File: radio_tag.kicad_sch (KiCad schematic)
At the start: 15 parts, among them U1 MICRF113, Y1 9M84375

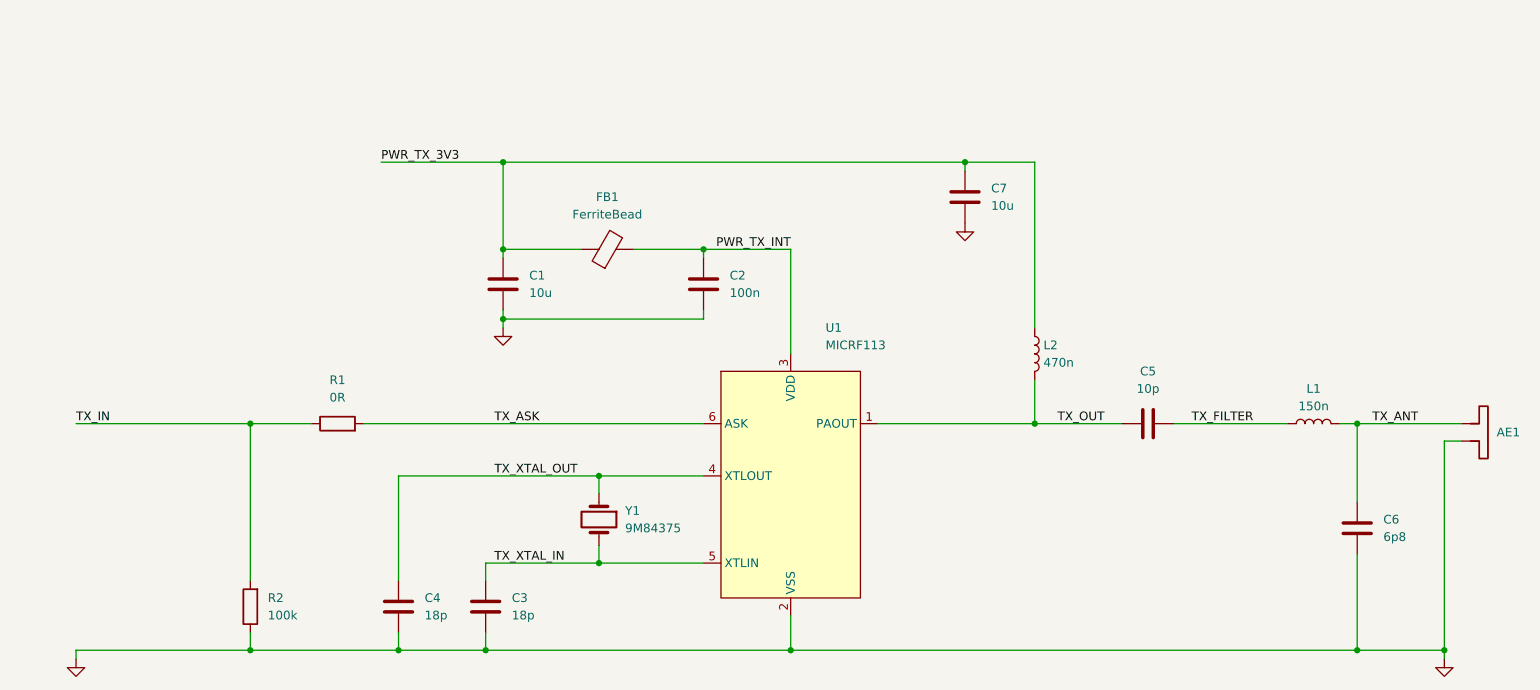
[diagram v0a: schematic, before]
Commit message: Add regulator and complete PN selection
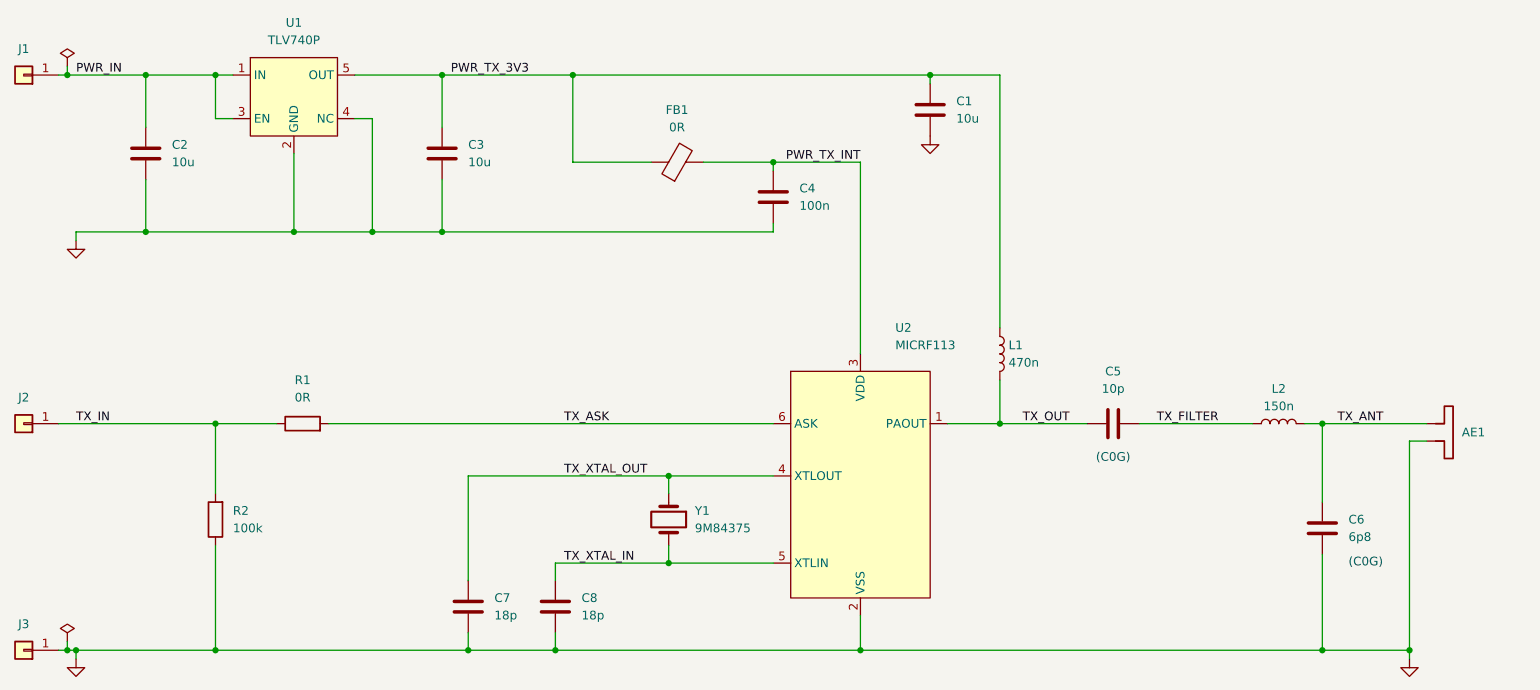
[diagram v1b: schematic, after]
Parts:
- removed C1: 10u, symbol Device:C
- added C2, C3: 10u, Capacitor_SMD:C_0805_2012Metric, symbol Device:C
- added J1, J2, J3: Conn_01x01, Connector_PinHeader_2.54mm:PinHeader_1x01_P2.54mm_Vertical, symbol Connector_Generic:Conn_01x01
- added U1: TLV740P, Package_TO_SOT_SMD:SOT-23-5, symbol regulators:TLV740P
- AE1: footprint (none) -> RF_Antenna:Texas_SWRA117D_2.4GHz_Left; now left out of the parts list
- C1: renamed from C7; footprint (none) -> Capacitor_SMD:C_0805_2012Metric; Manufacturer (none) -> Samsung Electro-mechanics; Manufacturer PN (none) -> CL21A106KOQNNNG; Supplier  (none) -> Digi-Key; Supplier PN (none) -> 1276-6455-1-ND
- C4: renamed from C2; footprint (none) -> Capacitor_SMD:C_0805_2012Metric; Manufacturer (none) -> YAGEO; Manufacturer PN (none) -> CC0805KRX7R9BB104; Supplier  (none) -> Digi-Key; Supplier PN (none) -> 311-1140-1-ND
- C5: footprint (none) -> Capacitor_SMD:C_0805_2012Metric; Manufacturer (none) -> Samsung Electro-mechanics; Manufacturer PN (none) -> CL21C100CBANNNC; Supplier  (none) -> Digi-Key; Supplier PN (none) -> 1276-2561-1-ND
- C6: footprint (none) -> Capacitor_SMD:C_0805_2012Metric; Manufacturer (none) -> YAGEO; Manufacturer PN (none) -> CC0805CRNPO9BN6R8; Supplier  (none) -> Digi-Key; Supplier PN (none) -> 311-1831-1-ND
- C7: renamed from C4; footprint (none) -> Capacitor_SMD:C_0805_2012Metric; Manufacturer (none) -> YAGEO; Manufacturer PN (none) -> CC0805JRNPO9BN180; Supplier  (none) -> Digi-Key; Supplier PN (none) -> 311-1102-1-ND
- C8: renamed from C3; footprint (none) -> Capacitor_SMD:C_0805_2012Metric; Manufacturer (none) -> YAGEO; Manufacturer PN (none) -> CC0805JRNPO9BN180; Supplier  (none) -> Digi-Key; Supplier PN (none) -> 311-1102-1-ND
- FB1: value FerriteBead -> 0R; footprint (none) -> Resistor_SMD:R_0805_2012Metric; Manufacturer (none) -> Stackpole Electronics; Manufacturer PN (none) -> RMCF0805ZT0R00; Supplier  (none) -> Digi-Key; Supplier PN (none) -> RMCF0805ZT0R00CT-ND
- L1: renamed from L2; footprint (none) -> Inductor_SMD:L_0805_2012Metric; Manufacturer (none) -> Murata Electronics; Manufacturer PN (none) -> LQW18ANR47J00D; Supplier  (none) -> Digi-Key; Supplier PN (none) -> 490-1184-1-ND
- L2: renamed from L1; footprint (none) -> Inductor_SMD:L_0805_2012Metric; Manufacturer (none) -> Pulse Electronics; Manufacturer PN (none) -> BSCH00100505R15JCS; Supplier  (none) -> Digi-Key; Supplier PN (none) -> 553-BSCH00100505R15JCSCT-ND
- R1: footprint (none) -> Resistor_SMD:R_0805_2012Metric; Manufacturer (none) -> Stackpole Electronics; Manufacturer PN (none) -> RMCF0805ZT0R00; Supplier  (none) -> Digi-Key; Supplier PN (none) -> RMCF0805ZT0R00CT-ND
- R2: footprint (none) -> Resistor_SMD:R_0805_2012Metric; Manufacturer (none) -> Stackpole Electronics; Manufacturer PN (none) -> RMCF0805JT100K; Supplier  (none) -> Digi-Key; Supplier PN (none) -> RMCF0805JT100KCT-ND
- U2: renamed from U1; Manufacturer (none) -> Microchip Technology; Manufacturer PN (none) -> MICRF113YM6-TR; Supplier  (none) -> Digi-Key; Supplier PN (none) -> 576-3229-1-ND
- Y1: footprint (none) -> Crystal:Crystal_SMD_HC49-SD; Manufacturer (none) -> ECS; Manufacturer PN (none) -> ECS-98.4375-CDX-0314-TR; Supplier  (none) -> Digi-Key; Supplier PN (none) -> XC1026CT-ND
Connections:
- net GND: now also C2.2, C3.2, J3.1 (Pin_1), U1.2 (GND), U1.4 (NC)
- net PWR_TX_3V3: now also C3.1, U1.5 (OUT)
- net TX_IN: now also J2.1 (Pin_1)
- new net PWR_IN: C2.1, J1.1 (Pin_1), U1.1 (IN), U1.3 (EN)
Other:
- note added: "(C0G)"
- moved on the sheet: AE1, C1, C4, C5, C6, C7, C8, FB1, L1, L2, R1, R2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

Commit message: Rough out component positions, remove incorrect antenna
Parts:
- AE1: footprint RF_Antenna:Texas_SWRA117D_2.4GHz_Left -> (none)
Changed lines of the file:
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@@
 			)
 		)
-		(property "Footprint" "RF_Antenna:Texas_SWRA117D_2.4GHz_Left"
+		(property "Footprint" ""
 			(at 252.73 100.33 0)
 			(effects

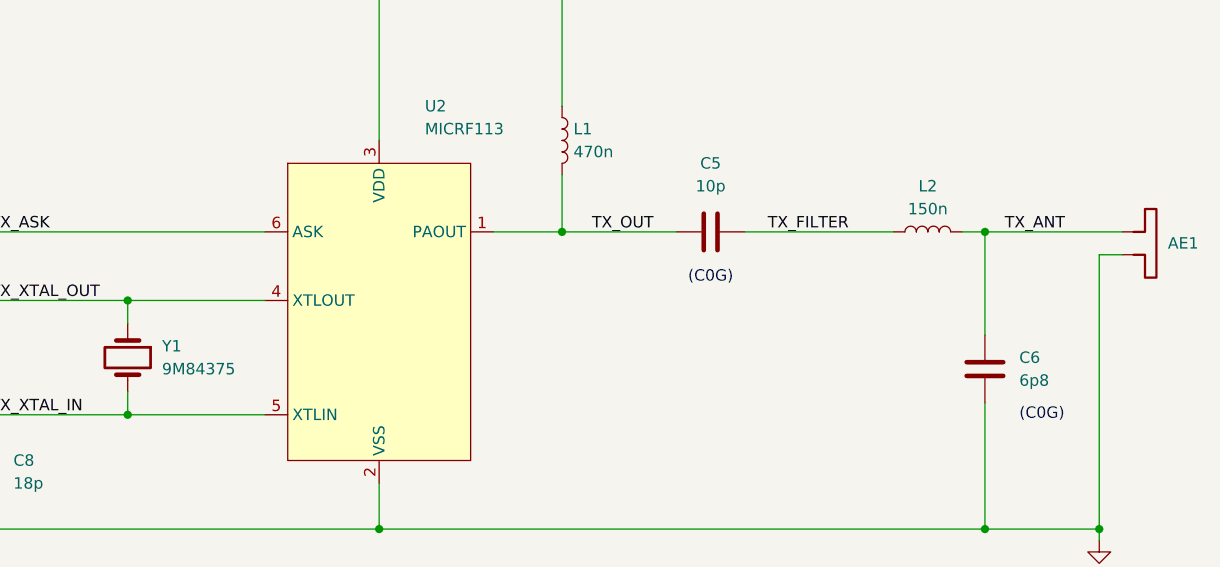
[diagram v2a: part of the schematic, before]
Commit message: Switch component values for 433 MHz operation
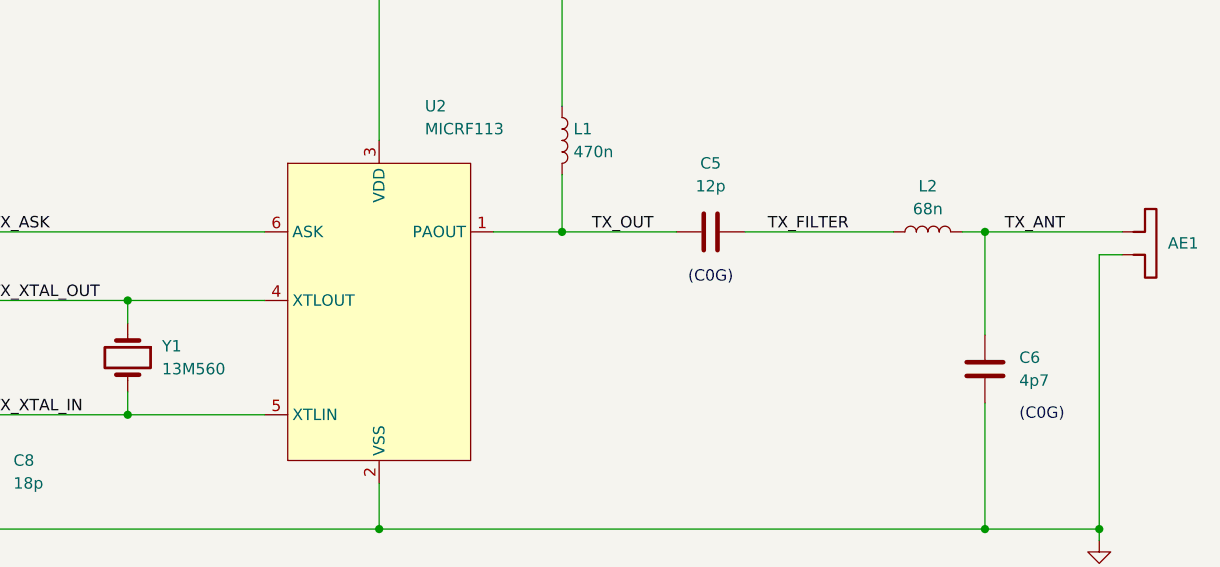
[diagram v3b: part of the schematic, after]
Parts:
- C5: value 10p -> 12p; Manufacturer Samsung Electro-mechanics -> Cal-Chip Electronics; Manufacturer PN CL21C100CBANNNC -> CHV0805N250120FCT; Supplier PN 1276-2561-1-ND -> 4713-CHV0805N250120FCT-ND
- C6: value 6p8 -> 4p7; Manufacturer YAGEO -> Cal-Chip Electronics; Manufacturer PN CC0805CRNPO9BN6R8 -> CHV0805N2504R7CCT; Supplier PN 311-1831-1-ND -> 4713-CHV0805N2504R7CCT-ND
- L2: value 150n -> 68n; Manufacturer Pulse Electronics -> Johanson Technology; Manufacturer PN BSCH00100505R15JCS -> LRC0603CJ68NGV001T; Supplier PN 553-BSCH00100505R15JCSCT-ND -> 712-LRC0603CJ68NGV001TCT-ND
- Y1: value 9M84375 -> 13M560; Manufacturer ECS -> Abracon; Manufacturer PN ECS-98.4375-CDX-0314-TR -> ABLS-13.560MHZ-10-R20-D-T; Supplier PN XC1026CT-ND -> 535-9687-1-ND
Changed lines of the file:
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@@
 			)
 		)
-		(property "Value" "10p"
+		(property "Value" "12p"
 			(at 201.93 95.25 90)
 			(effects
@@
 			)
 		)
-		(property "Manufacturer" "Samsung Electro-mechanics"
+		(property "Manufacturer" "Cal-Chip Electronics"
 			(at 201.93 100.33 0)
 			(effects
@@
 			)
 		)
-		(property "Manufacturer PN" "CL21C100CBANNNC"
+		(property "Manufacturer PN" "CHV0805N250120FCT"
 			(at 201.93 100.33 0)
 			(effects
@@
 			)
 		)
-		(property "Supplier PN" "1276-2561-1-ND"
+		(property "Supplier PN" "4713-CHV0805N250120FCT-ND"
 			(at 201.93 100.33 0)
 			(effects
@@
 			)
 		)
-		(property "Value" "6p8"
+		(property "Value" "4p7"
 			(at 236.22 116.8399 0)
 			(effects
@@
 			)
 		)
-		(property "Manufacturer" "YAGEO"
+		(property "Manufacturer" "Cal-Chip Electronics"
 			(at 232.41 115.57 0)
 			(effects
@@
 			)
 		)
-		(property "Manufacturer PN" "CC0805CRNPO9BN6R8"
+		(property "Manufacturer PN" "CHV0805N2504R7CCT"
 			(at 232.41 115.57 0)
 			(effects
@@
 			)
 		)
-		(property "Supplier PN" "311-1831-1-ND"
+		(property "Supplier PN" "4713-CHV0805N2504R7CCT-ND"
 			(at 232.41 115.57 0)
 			(effects
@@
 			)
 		)
-		(property "Value" "9M84375"
+		(property "Value" "13M560"
 			(at 140.97 115.5699 90)
 			(effects
@@
 			)
 		)
-		(property "Manufacturer" "ECS"
+		(property "Manufacturer" "Abracon"
 			(at 137.16 114.3 90)
 			(effects
@@
 			)
 		)
-		(property "Manufacturer PN" "ECS-98.4375-CDX-0314-TR"
+		(property "Manufacturer PN" "ABLS-13.560MHZ-10-R20-D-T"
 			(at 137.16 114.3 90)
 			(effects
@@
 			)
 		)
-		(property "Supplier PN" "XC1026CT-ND"
+		(property "Supplier PN" "535-9687-1-ND"
 			(at 137.16 114.3 90)
 			(effects
@@
 			)
 		)
-		(property "Value" "150n"
+		(property "Value" "68n"
 			(at 226.06 97.79 90)
 			(effects
@@
 			)
 		)
-		(property "Manufacturer" "Pulse Electronics"
+		(property "Manufacturer" "Johanson Technology"
 			(at 226.06 100.33 0)
 			(effects
@@
 			)
 		)
-		(property "Manufacturer PN" "BSCH00100505R15JCS"
+		(property "Manufacturer PN" "LRC0603CJ68NGV001T"
 			(at 226.06 100.33 0)
 			(effects
@@
 			)
 		)
-		(property "Supplier PN" "553-BSCH00100505R15JCSCT-ND"
+		(property "Supplier PN" "712-LRC0603CJ68NGV001TCT-ND"
 			(at 226.06 100.33 0)
 			(effects

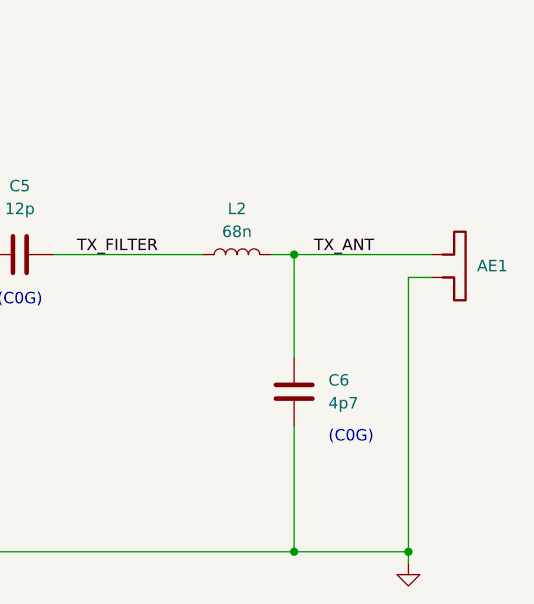
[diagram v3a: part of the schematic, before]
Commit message: Select new antenna and add to layout
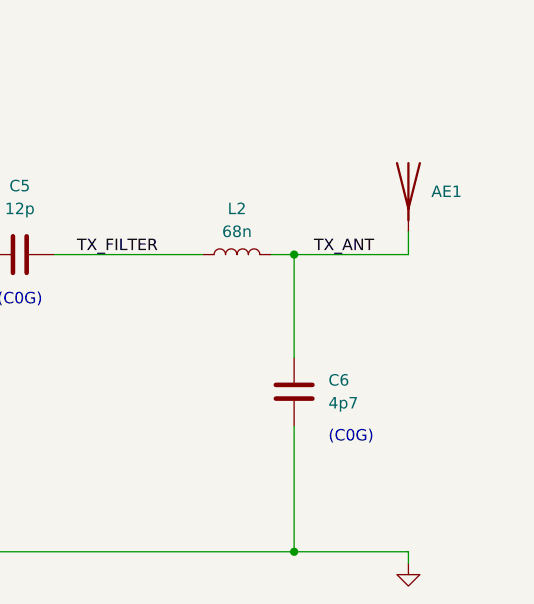
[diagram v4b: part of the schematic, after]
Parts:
- AE1: footprint (none) -> rf:TE_ANT-433-HETH; symbol Device:Antenna_Dipole -> Device:Antenna; Manufacturer (none) -> TE Connectivity; Manufacturer PN (none) -> ANT-433-HETH; Supplier  (none) -> Digi-Key; Supplier PN (none) -> ANT-433-HETH-ND; now in the parts list
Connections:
- net GND: no longer AE1.2
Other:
- moved on the sheet: AE1
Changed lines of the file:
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@@
-	)
-	(junction
-		(at 245.11 133.35)
-		(diameter 0)
-		(color 0 0 0 0)
 	)
 	(junction
@@
 	(wire
 		(pts
-			(xy 247.65 102.87) (xy 245.11 102.87)
+			(xy 245.11 97.79) (xy 245.11 100.33)
 		)
 		(stroke
@@
 	(wire
 		(pts
-			(xy 232.41 100.33) (xy 247.65 100.33)
+			(xy 232.41 100.33) (xy 245.11 100.33)
 		)
 		(stroke
@@
 		(pts
 			(xy 232.41 119.38) (xy 232.41 133.35)
-		)
-		(stroke
-			(width 0)
-			(type default)
-		)
-	)
-	(wire
-		(pts
-			(xy 245.11 102.87) (xy 245.11 133.35)
 		)
 		(stroke
@@
 	)
 	(symbol
-		(lib_id "Device:Antenna_Dipole")
-		(at 252.73 100.33 270)
+		(lib_id "Device:Antenna")
+		(at 245.11 92.71 0)
 		(unit 1)
 		(exclude_from_sim no)
-		(in_bom no)
+		(in_bom yes)
 		(on_board yes)
 		(dnp no)
 		(fields_autoplaced yes)
 		(property "Reference" "AE1"
-			(at 252.73 101.5999 90)
+			(at 247.65 93.3449 0)
 			(effects
 				(font
@@
 		)
 		(property "Value" "Antenna_Dipole"
-			(at 252.73 102.8699 90)
+			(at 247.6499 92.71 90)
 			(effects
 				(font
@@
 			)
 		)
-		(property "Footprint" ""
-			(at 252.73 100.33 0)
+		(property "Footprint" "rf:TE_ANT-433-HETH"
+			(at 245.11 92.71 0)
 			(effects
 				(font
@@
 		)
 		(property "Datasheet" "~"
-			(at 252.73 100.33 0)
-			(effects
-				(font
-					(size 1.27 1.27)
-				)
-				(hide yes)
-			)
-		)
-		(property "Description" "Dipole antenna"
-			(at 252.73 100.33 0)
-			(effects
-				(font
-					(size 1.27 1.27)
-				)
-				(hide yes)
-			)
-		)
-		(property "Supplier " "~"
-			(at 252.73 100.33 0)
-			(effects
-				(font
-					(size 1.27 1.27)
-				)
-				(hide yes)
-			)
-		)
-		(property "Manufacturer" "~"
-			(at 252.73 100.33 0)
-			(effects
-				(font
-					(size 1.27 1.27)
-				)
-				(hide yes)
-			)
-		)
-		(property "Manufacturer PN" "~"
-			(at 252.73 100.33 0)
-			(effects
-				(font
-					(size 1.27 1.27)
-				)
-				(hide yes)
-			)
-		)
-		(property "Supplier PN" "~"
-			(at 252.73 100.33 0)
-			(effects
-				(font
-					(size 1.27 1.27)
-				)
-				(hide yes)
-			)
-		)
-		(pin "2"
+			(at 245.11 92.71 0)
+			(effects
+				(font
+					(size 1.27 1.27)
+				)
+				(hide yes)
+			)
+		)
+		(property "Description" "Antenna"
+			(at 245.11 92.71 0)
+			(effects
+				(font
+					(size 1.27 1.27)
+				)
+				(hide yes)
+			)
+		)
+		(property "Supplier " "Digi-Key"
+			(at 245.11 92.71 0)
+			(effects
+				(font
+					(size 1.27 1.27)
+				)
+				(hide yes)
+			)
+		)
+		(property "Manufacturer" "TE Connectivity"
+			(at 245.11 92.71 0)
+			(effects
+				(font
+					(size 1.27 1.27)
+				)
+				(hide yes)
+			)
+		)
+		(property "Manufacturer PN" "ANT-433-HETH"
+			(at 245.11 92.71 0)
+			(effects
+				(font
+					(size 1.27 1.27)
+				)
+				(hide yes)
+			)
+		)
+		(property "Supplier PN" "ANT-433-HETH-ND"
+			(at 245.11 92.71 0)
+			(effects
+				(font
+					(size 1.27 1.27)
+				)
+				(hide yes)
+			)
 		)
 		(pin "1"
